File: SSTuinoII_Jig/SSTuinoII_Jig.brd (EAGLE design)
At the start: 73.6 x 73.3 mm, 13 parts, among them J1 MuseLab CMSIS-DAP, Q1 BS170

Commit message: finalised test jig
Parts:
- removed J2, J3: (no value), OPL_Connector:H2-2.54
- added ESPRX_J, ESPTX_J: (no value), OPL_Connector:H2-2.54
- added S1: (no value), SparkFun-Switches:SWITCH_SPDT_PTH_11.6X4.0MM_KIT
- J1: value MuseLab CMSIS-DAP -> MuseLab CMSIS-DAP Only
- moved R3 59.7 mm to (3.81, 44.5), turned to 270 degrees
- moved POWER 58.9 mm to (10.5, 27.6), turned to 270 degrees
- moved R2 56.2 mm to (7.62, 54.6), turned to 180 degrees
- moved J1 56.1 mm to (6.35, 12.7), turned to 0 degrees
- moved LS1 55.3 mm to (6.99, 63.5), turned to 90 degrees
- moved R1 51.2 mm to (10.5, 35.9), turned to 90 degrees
- moved Q1 45.8 mm to (8.89, 48.3), turned to 180 degrees
- moved U$2 19.1 mm to (66.0, 11.4)
- moved ESP_IO0 18.9 mm to (74.9, 41.9), turned to 270 degrees
- moved ESP_RESET 18.5 mm to (74.9, 30.5), turned to 270 degrees
- moved U$1 14.0 mm to (17.8, 59.7)
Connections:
- new net PWR: J1.10, S1.2
- net 5V: now also S1.1; no longer J1.10
- net ESP_RX: now also ESPRX_J.2; no longer J3.2
- net ESP_TX: now also ESPTX_J.2; no longer J2.2
- net GND: now also U$1.P$25
- net MEGA_RX: now also ESPTX_J.1; no longer J2.1
- net MEGA_TX: now also ESPRX_J.1; no longer J3.1
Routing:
- net ESP_IO0: track 0.00 -> 151.9 mm
- net 3.3V: track 0.00 -> 103.9 mm
- net MEGA_D5: track 0.00 -> 97.3 mm
- net 5V: track 0.00 -> 77.0 mm
- net ESP_EN: track 0.00 -> 66.1 mm
- net SWCLK: track 0.00 -> 56.2 mm
- net SWDIO: track 0.00 -> 49.9 mm
- net MEGA_D4: track 0.00 -> 48.7 mm
- net NRST: track 0.00 -> 46.6 mm
- net PWR: track 0.00 -> 37.3 mm
- net MEGA_TX: track 0.00 -> 25.6 mm
- net ESP_TX: track 0.00 -> 23.8 mm
- net ESP_RX: track 0.00 -> 16.1 mm
- net MEGA_RX: track 0.00 -> 15.0 mm
- net N$1: track 0.00 -> 3.18 mm
- added copper zone on layer 16, net GND
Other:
- board size 73.6 x 73.3 mm -> 80 x 71.1 mm
- board text added: "+"
- board text added: "3V3"
- board text added: "5V"
- board text added: "CLK"
- board text added: "DIO"
- board text added: "GND"
- board text added: "SSTuino II Test Jig RevA 2021 Dec"
- board text added: "USB Port facing this way"
- board text removed: "SSTuino II Test Jig RevA 2021 Nov"

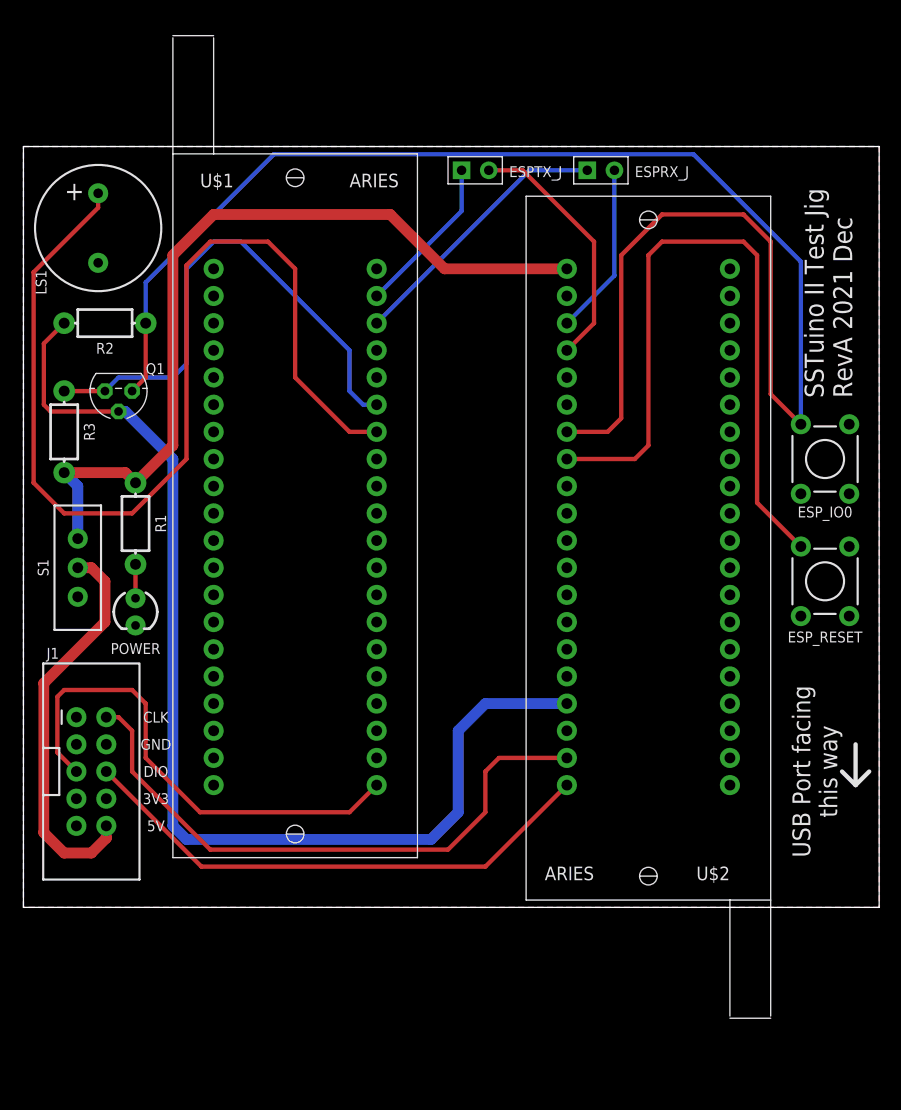
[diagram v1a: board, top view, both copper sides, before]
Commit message: final version of the revA jig, revB incoming soon
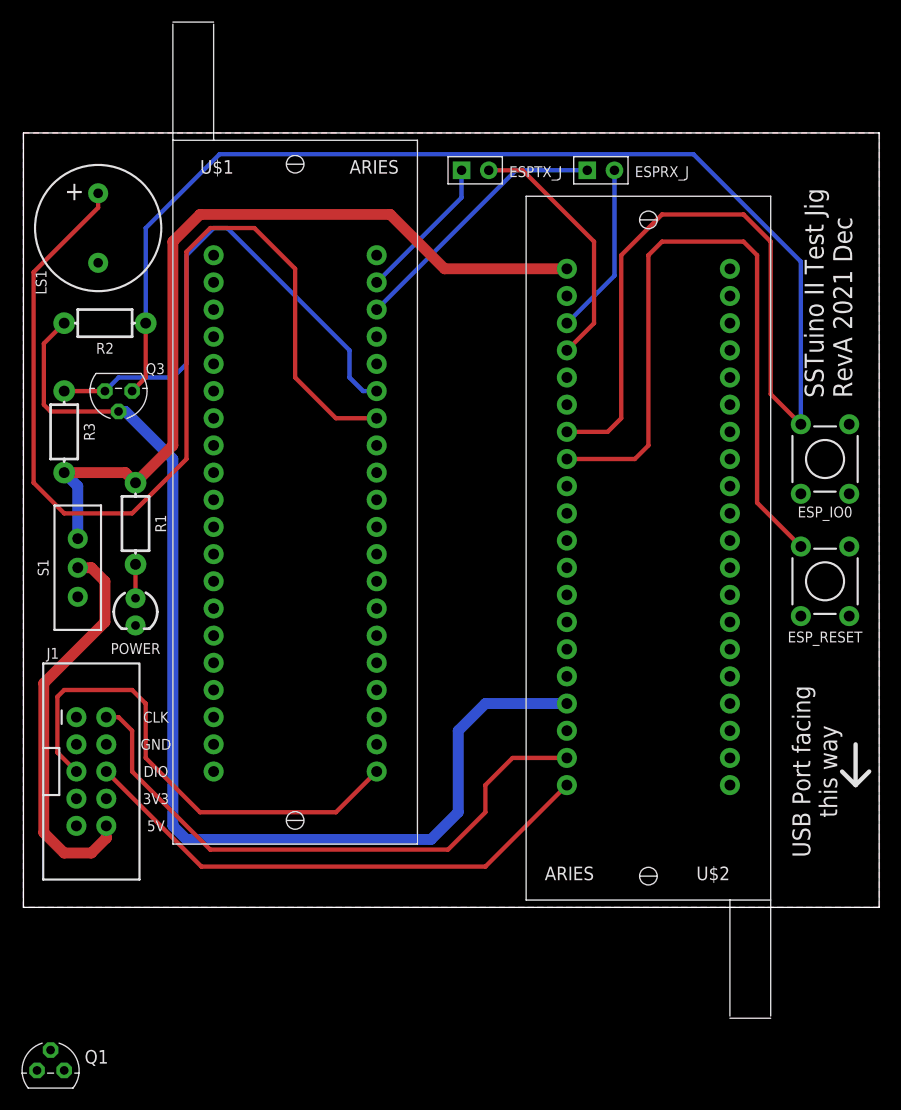
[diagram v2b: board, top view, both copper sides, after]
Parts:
- added Q3: BS170, Transistor:TO92
- Q1: value BS170 -> BSS101; device Transistor:TO92 -> transistor-fet:TO92
- moved Q1 63.8 mm to (2.54, -15.2), turned to 0 degrees
- moved U$1 1.27 mm to (17.8, 61.0)
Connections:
- net 3.3V: now also Q3.2; no longer Q1.2
- net ESP_IO0: now also Q3.3; no longer Q1.3
- net MEGA_D4: now also Q3.1; no longer Q1.1
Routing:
- net ESP_IO0: track 151.9 -> 154.9 mm
- net MEGA_RX: track 15.0 -> 13.8 mm
- net MEGA_D5: track 97.3 -> 98.5 mm
- net SWCLK: track 56.2 -> 55.5 mm
- net 5V: track 77.0 -> 77.7 mm
- net MEGA_TX: track 25.6 -> 25.1 mm
- net MEGA_D4: track 48.7 -> 49.3 mm
- net NRST: track 46.6 -> 47.1 mm
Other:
- board size 80 x 71.1 mm -> 80 x 72.4 mm

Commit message: updated test jig
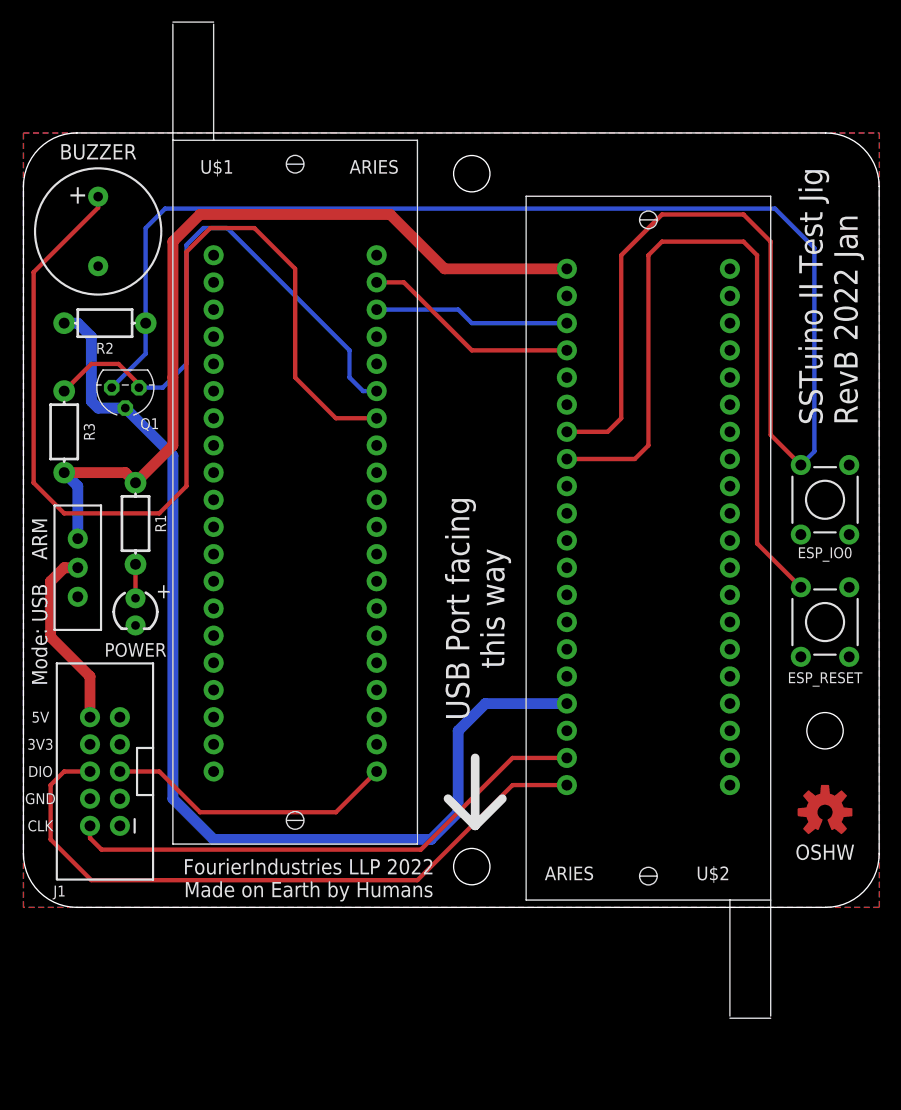
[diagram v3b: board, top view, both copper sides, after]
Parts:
- removed ESPRX_J, ESPTX_J: (no value), OPL_Connector:H2-2.54
- removed LS1: BUZZER-PTH_KIT, SparkFun-Electromechanical:BUZZER-12MM-KIT
- removed Q3: BS170, Transistor:TO92
- added BUZZER: BUZZER-PTH_KIT, SparkFun-Electromechanical:BUZZER-12MM-KIT
- added U$3: (no value), D3ltav's Custom:OSHW-LOGO-M_COPPER-SOLDERMASK
- Q1: value BSS101 -> BS170
- moved Q1 64.2 mm to (9.53, 48.6), turned to 180 degrees
- moved ESP_RESET 3.81 mm to (74.9, 26.7)
- moved ESP_IO0 3.81 mm to (74.9, 38.1)
- moved J1 1.27 mm to (7.62, 12.7), turned to 180 degrees
- renumbered S1 to MODE
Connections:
- removed net ESP_RX: ESPRX_J.2, U$2.P$23
- removed net ESP_TX: ESPTX_J.2, U$2.P$24
- net 3.3V: now also Q1.2; no longer Q3.2
- net ESP_IO0: now also Q1.1; no longer Q3.3
- net GND: now also BUZZER.-; no longer LS1.-
- net MEGA_D4: now also Q1.3; no longer Q3.1
- net MEGA_D5: now also BUZZER.+; no longer LS1.+
- net MEGA_RX: now also U$2.P$24; no longer ESPTX_J.1
- net MEGA_TX: now also U$2.P$23; no longer ESPRX_J.1
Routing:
- net ESP_TX: track 23.8 -> 0.00 mm
- net PWR: track 37.3 -> 17.3 mm
- net NRST: track 47.1 -> 27.2 mm
- net ESP_RX: track 16.1 -> 0.00 mm
- net SWDIO: track 49.9 -> 62.8 mm
- net MEGA_TX: track 25.1 -> 18.3 mm
- net MEGA_RX: track 13.8 -> 20.4 mm
- net ESP_IO0: track 154.9 -> 161.3 mm
- net SWCLK: track 55.5 -> 49.7 mm
- net 3.3V: track 103.9 -> 99.0 mm
- net ESP_EN: track 66.1 -> 69.9 mm
- net MEGA_D4: track 49.3 -> 51.9 mm
- net MEGA_D5: track 98.5 -> 99.7 mm
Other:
- outline, holes or cut-outs redrawn
- board text added: "FourierIndustries LLP 2022 Made on Earth by Humans"
- board text added: "Mode: USB ARM"
- board text added: "OSHW"
- board text added: "SSTuino II Test Jig RevB 2022 Jan"
- board text removed: "SSTuino II Test Jig RevA 2021 Dec"
